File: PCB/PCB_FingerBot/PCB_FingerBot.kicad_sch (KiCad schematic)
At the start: 9 parts, among them J1 Conn_01x02_Pin, J2 Conn_2_pads, J3 Conn_01x03_Pin, U1 XIAO-ESP32-C6-SMD, U2 TPS61222DCK

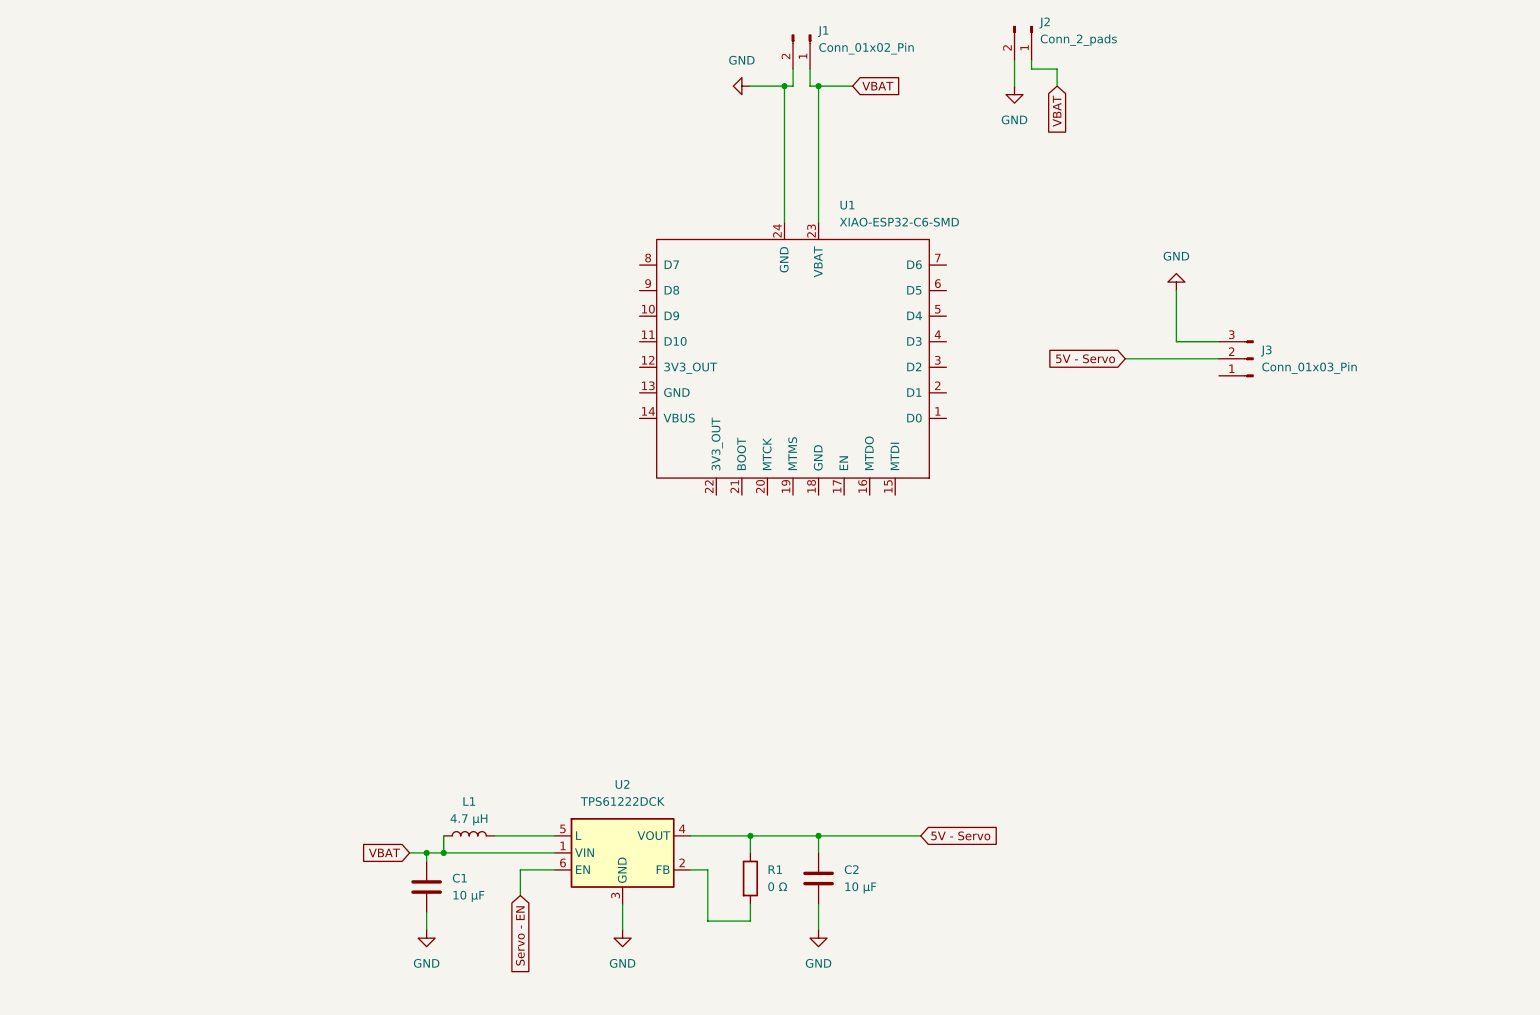
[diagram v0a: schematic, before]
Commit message: Changed boost converter to a more powerful one
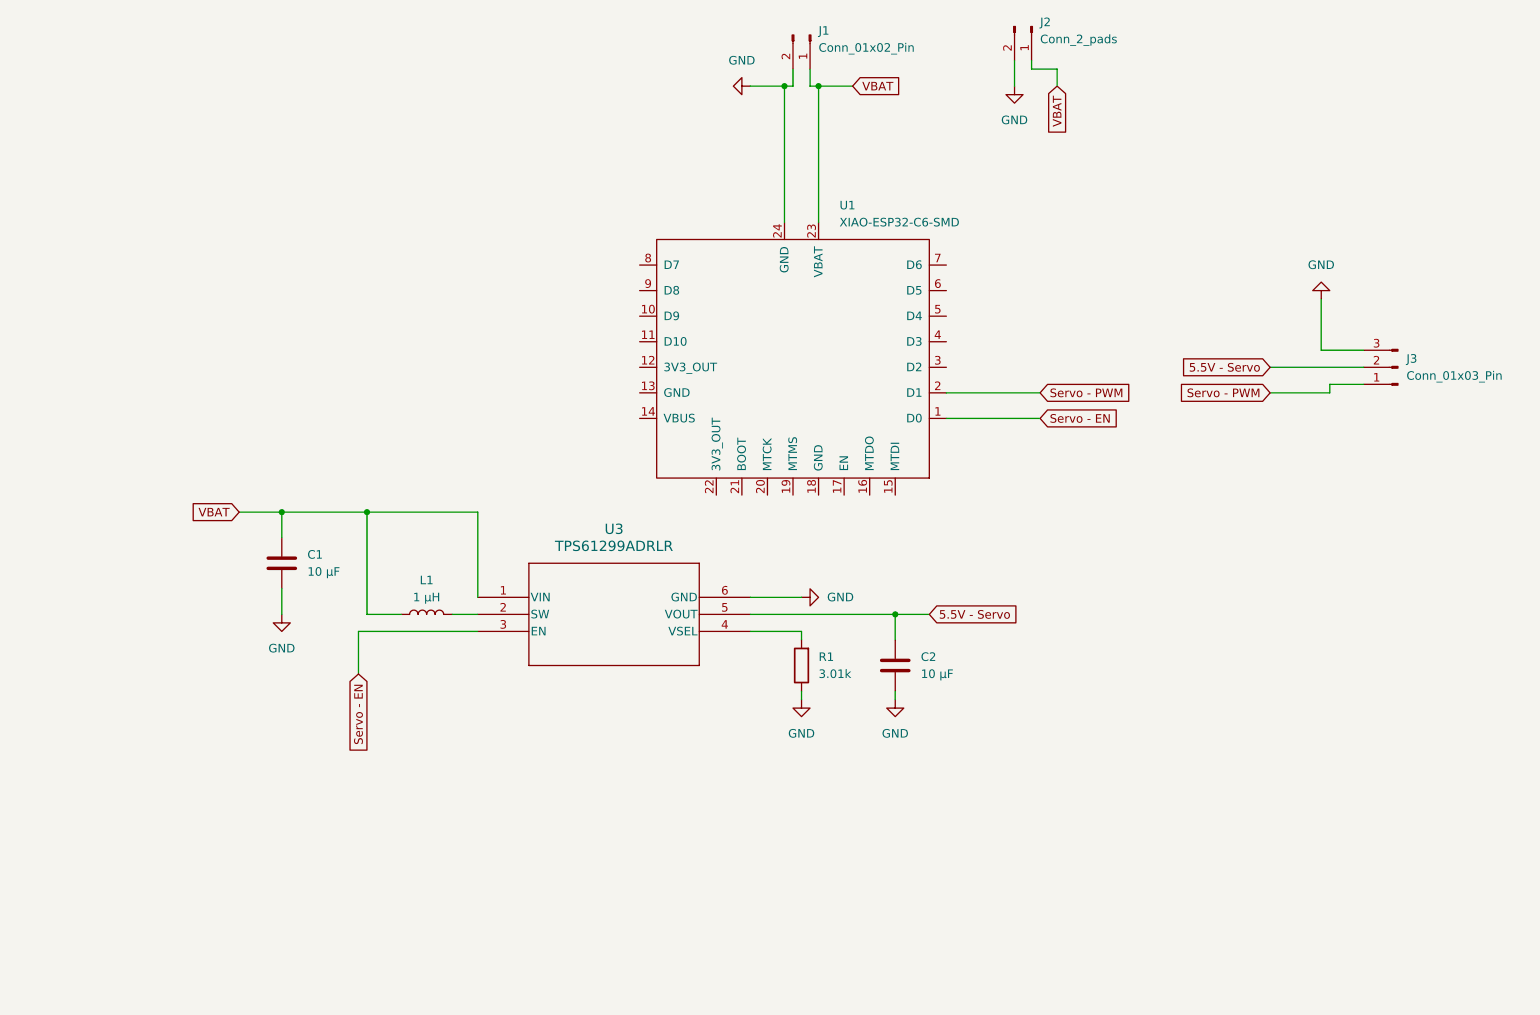
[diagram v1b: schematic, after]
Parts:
- removed U2: TPS61222DCK, Package_TO_SOT_SMD:Texas_R-PDSO-G6, symbol Regulator_Switching:TPS61222DCK
- added U3: TPS61299ADRLR, TPS61299:SOT-5X3-6_DRL_TEX, symbol TPS61299:TPS61299ADRLR
- L1: value 4.7 μH -> 1 μH
- R1: value 0 Ω -> 3.01k
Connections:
- net GND: now also R1.1, U3.6 (GND)
- net Servo - EN: now also U1.1 (D0), U3.3 (EN)
- net VBAT: now also U3.1 (VIN)
- net Servo - PWM: now reaches J3.1 (Pin_1)
- net Servo - PWM: now also U1.2 (D1)
- net at R1.2: now also U3.4 (VSEL)
- net at L1.2: now also U3.2 (SW)
- net 5V - Servo renamed 5.5V - Servo
- net 5.5V - Servo: now also U3.5 (VOUT); no longer R1.1
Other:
- moved on the sheet: J3

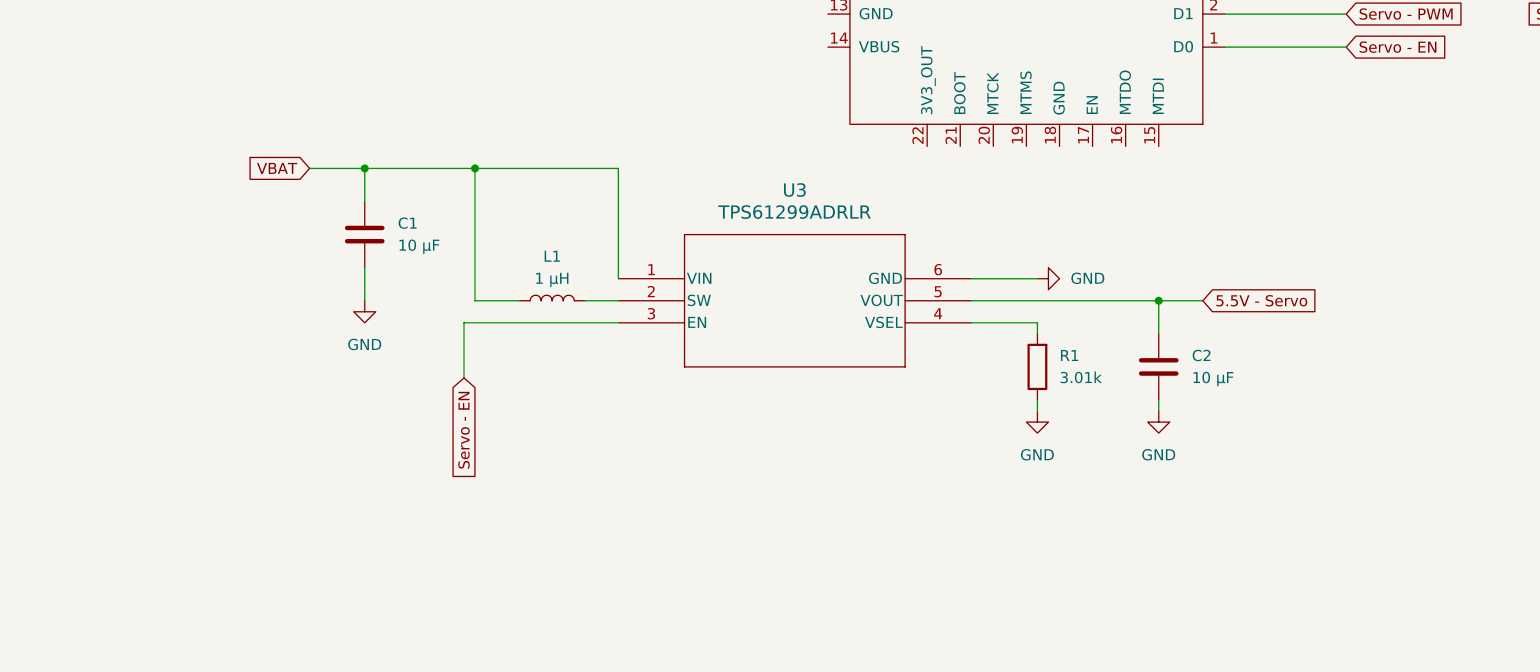
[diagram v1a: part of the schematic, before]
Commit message: Update component to JLC available ones
Changed boost converter to an available reference on jlc, changed SEEED studio for through hole soldering (part not available on JLC), started other part assigne
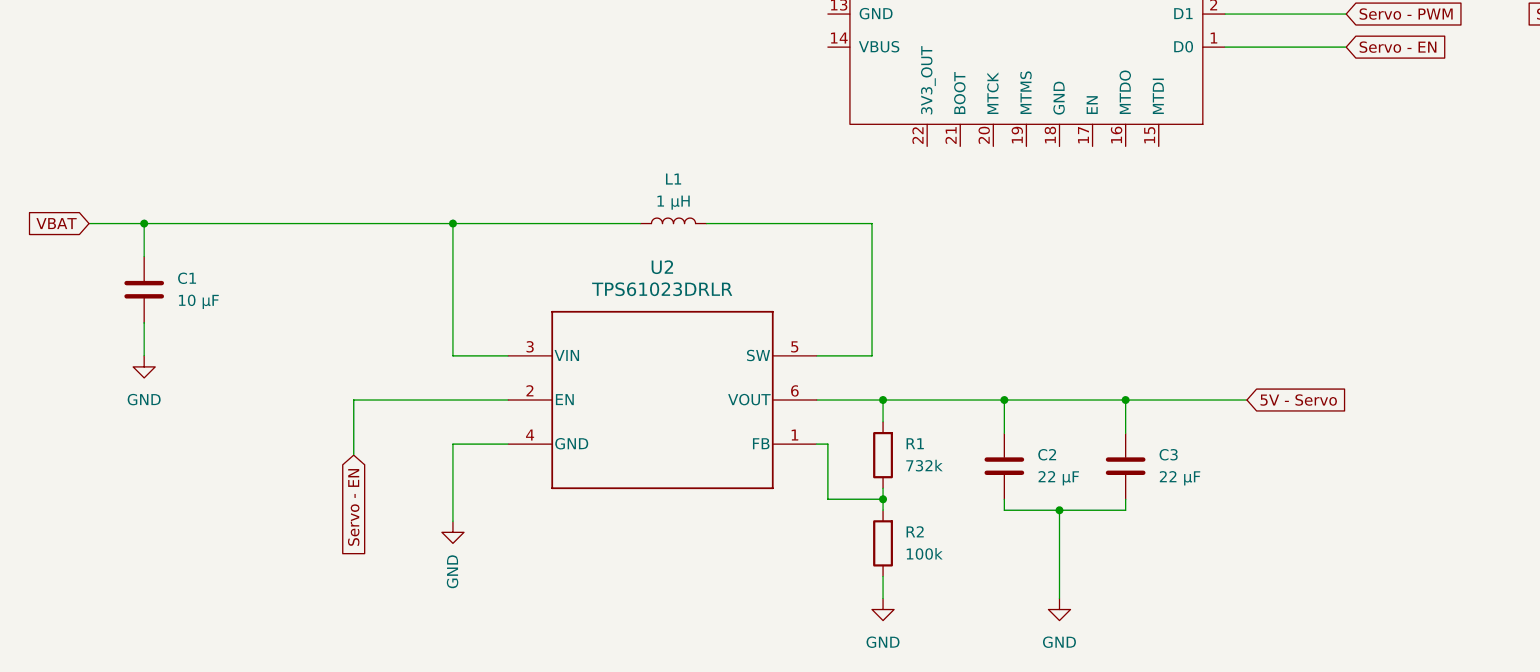
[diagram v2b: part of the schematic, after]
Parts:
- removed U3: TPS61299ADRLR, TPS61299:SOT-5X3-6_DRL_TEX, symbol TPS61299:TPS61299ADRLR
- added C3: 22 μF, Capacitor_SMD:C_0805_2012Metric, symbol Device:C
- added R2: 100k, symbol Device:R
- added U2: TPS61023DRLR, TPS61023DRLR:DRL0006A, symbol TPS61023DRLR:TPS61023DRLR
- C1: footprint (none) -> Capacitor_SMD:C_0603_1608Metric; LCSC (none) -> C96446
- C2: value 10 μF -> 22 μF; footprint (none) -> Capacitor_SMD:C_0805_2012Metric; LCSC (none) -> C5366742
- J1: footprint Connector_JST:JST_XH_B2B-XH-AM_1x02_P2.50mm_Vertical -> Connector_JST:JST_PH_B2B-PH-K_1x02_P2.00mm_Vertical; LCSC (none) -> C131337
- L1: footprint (none) -> Inductor_SMD:L_1008_2520Metric; LCSC (none) -> C86091
- R1: value 3.01k -> 732k
- U1: footprint Seeed_Studio_XIAO_Series:XIAO-ESP32-C6-SMD -> Seeed_Studio_XIAO_Series:XIAO-ESP32-C6-DIP
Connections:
- net 5.5V - Servo: no longer C2.1
- net GND: now also C3.2, R2.1, U2.4 (GND); no longer R1.1
- net Servo - EN: now also U2.2 (EN)
- net VBAT: now also U2.3 (VIN)
- net at L1.2: now also U2.5 (SW)
- net 5V - Servo: now reaches R1.2
- net 5V - Servo: now also C2.1, C3.1, U2.6 (VOUT)
- new net: R1.1, R2.2, U2.1 (FB)
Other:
- moved on the sheet: C1, C2, L1, R1

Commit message: Added headers for SEEED, changed components and footprints
Added mouting female pin headers on SEEED footprint, modified the passive components of the power converter, modified footprint of inductor to spec
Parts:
- J3: footprint (none) -> Connector_PinHeader_2.54mm:PinHeader_1x03_P2.54mm_Vertical; LCSC (none) -> C49257
- L1: value 1 μH -> 2.7 μH; footprint Inductor_SMD:L_1008_2520Metric -> Inductor_SMD:L_6.3x6.3_H3; LCSC C86091 -> C3222940
- R1: footprint (none) -> Resistor_SMD:R_0201_0603Metric; LCSC (none) -> C246003
- R2: footprint (none) -> Resistor_SMD:R_0402_1005Metric; LCSC (none) -> C481918
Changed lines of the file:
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@@
 			)
 		)
-		(property "Footprint" ""
+		(property "Footprint" "Resistor_SMD:R_0201_0603Metric"
 			(at 122.428 156.21 90)
 			(hide yes)
@@
 		)
 		(property "Description" "Resistor"
+			(at 120.65 156.21 0)
+			(hide yes)
+			(show_name no)
+			(do_not_autoplace no)
+			(effects
+				(font
+					(size 1.27 1.27)
+				)
+			)
+		)
+		(property "LCSC" "C246003"
 			(at 120.65 156.21 0)
 			(hide yes)
@@
 			)
 		)
-		(property "Footprint" ""
+		(property "Footprint" "Connector_PinHeader_2.54mm:PinHeader_1x03_P2.54mm_Vertical"
 			(at 227.33 101.6 0)
 			(hide yes)
@@
 		)
 		(property "Description" "Generic connector, single row, 01x03, script generated"
+			(at 227.33 101.6 0)
+			(hide yes)
+			(show_name no)
+			(do_not_autoplace no)
+			(effects
+				(font
+					(size 1.27 1.27)
+				)
+			)
+		)
+		(property "LCSC" "C49257"
 			(at 227.33 101.6 0)
 			(hide yes)
@@
 			)
 		)
-		(property "Value" "1 μH"
+		(property "Value" "2.7 μH"
 			(at 96.52 127 90)
 			(show_name no)
@@
 			)
 		)
-		(property "Footprint" "Inductor_SMD:L_1008_2520Metric"
+		(property "Footprint" "Inductor_SMD:L_6.3x6.3_H3"
 			(at 96.52 129.54 0)
 			(hide yes)
@@
 			)
 		)
-		(property "Description" "LQM2HPN1R0MG0L"
+		(property "Description" "1255AY-2R7N=P3"
 			(at 96.52 129.54 0)
 			(hide yes)
@@
 			)
 		)
-		(property "LCSC" "C86091"
+		(property "LCSC" "C3222940"
 			(at 96.52 129.54 90)
 			(hide yes)
@@
 			)
 		)
-		(property "Footprint" ""
+		(property "Footprint" "Resistor_SMD:R_0402_1005Metric"
 			(at 122.428 166.37 90)
 			(hide yes)
@@
 			(at 120.65 166.37 0)
 			(hide yes)
+			(show_name no)
+			(do_not_autoplace no)
+			(effects
+				(font
+					(size 1.27 1.27)
+				)
+			)
+		)
+		(property "LCSC" "C481918"
+			(at 120.65 166.37 0)
+			(hide yes)

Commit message: Made a first PCB layout + corrected battery polarity on jst connect
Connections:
- net GND: now also J1.1 (Pin_1); no longer J1.2 (Pin_2)
- net VBAT: now also J1.2 (Pin_2); no longer J1.1 (Pin_1)
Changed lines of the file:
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@@
 	)
 	(junction
-		(at 135.89 59.69)
+		(at 135.89 69.85)
 		(diameter 0)
 		(color 0 0 0 0)
@@
 	(wire
 		(pts
-			(xy 139.7 59.69) (xy 139.7 57.15)
+			(xy 137.16 57.15) (xy 137.16 59.69)
 		)
 		(stroke
@@
 	(wire
 		(pts
-			(xy 137.16 59.69) (xy 137.16 57.15)
-		)
-		(stroke
-			(width 0)
-			(type default)
-		)
-	)
-	(wire
-		(pts
 			(xy 120.65 161.29) (xy 120.65 162.56)
 		)
@@
 	(wire
 		(pts
-			(xy 139.7 59.69) (xy 140.97 59.69)
+			(xy 137.16 59.69) (xy 140.97 59.69)
 		)
 		(stroke
@@
 	(wire
 		(pts
+			(xy 135.89 59.69) (xy 135.89 80.01)
+		)
+		(stroke
+			(width 0)
+			(type default)
+		)
+	)
+	(wire
+		(pts
 			(xy 77.47 144.78) (xy 71.12 144.78)
 		)
@@
 	(wire
 		(pts
-			(xy 135.89 59.69) (xy 137.16 59.69)
+			(xy 135.89 69.85) (xy 139.7 69.85)
 		)
 		(stroke
@@
 	(wire
 		(pts
+			(xy 139.7 57.15) (xy 139.7 69.85)
+		)
+		(stroke
+			(width 0)
+			(type default)
+		)
+	)
+	(wire
+		(pts
 			(xy 130.81 59.69) (xy 135.89 59.69)
 		)
@@
 		)
 		(stroke
-			(width 0)
-			(type default)
-		)
-	)
-	(wire
-		(pts
-			(xy 135.89 59.69) (xy 135.89 80.01)
-		)
-		(stroke
